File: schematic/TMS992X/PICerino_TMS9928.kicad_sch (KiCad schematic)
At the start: 75 parts, among them CON1 PICERINO-EDGE, J1 Conn_01x02, J10 Conn_01x03, J2 Conn_01x03, J3 Conn_01x03, J4 Conn_01x03, J5 Y, J6 Yr, J7 Yb, J8 Conn_01x08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

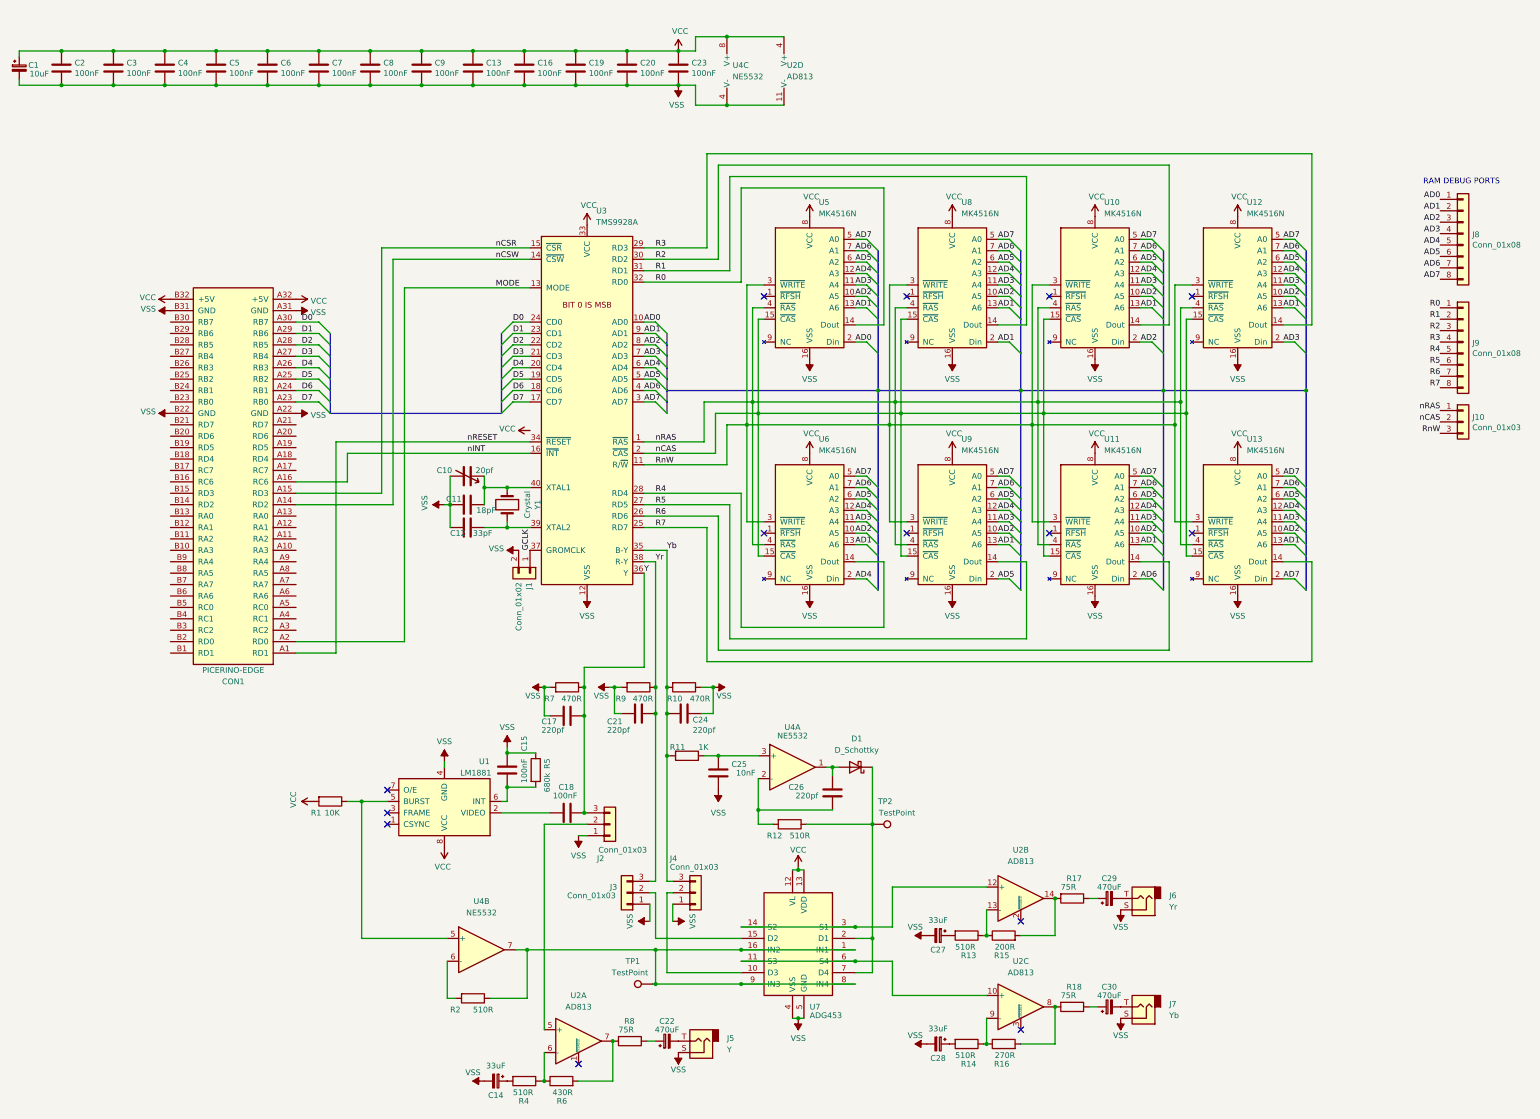
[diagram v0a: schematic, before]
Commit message: added new switch and sample video chip to simplify video output. work in progress.
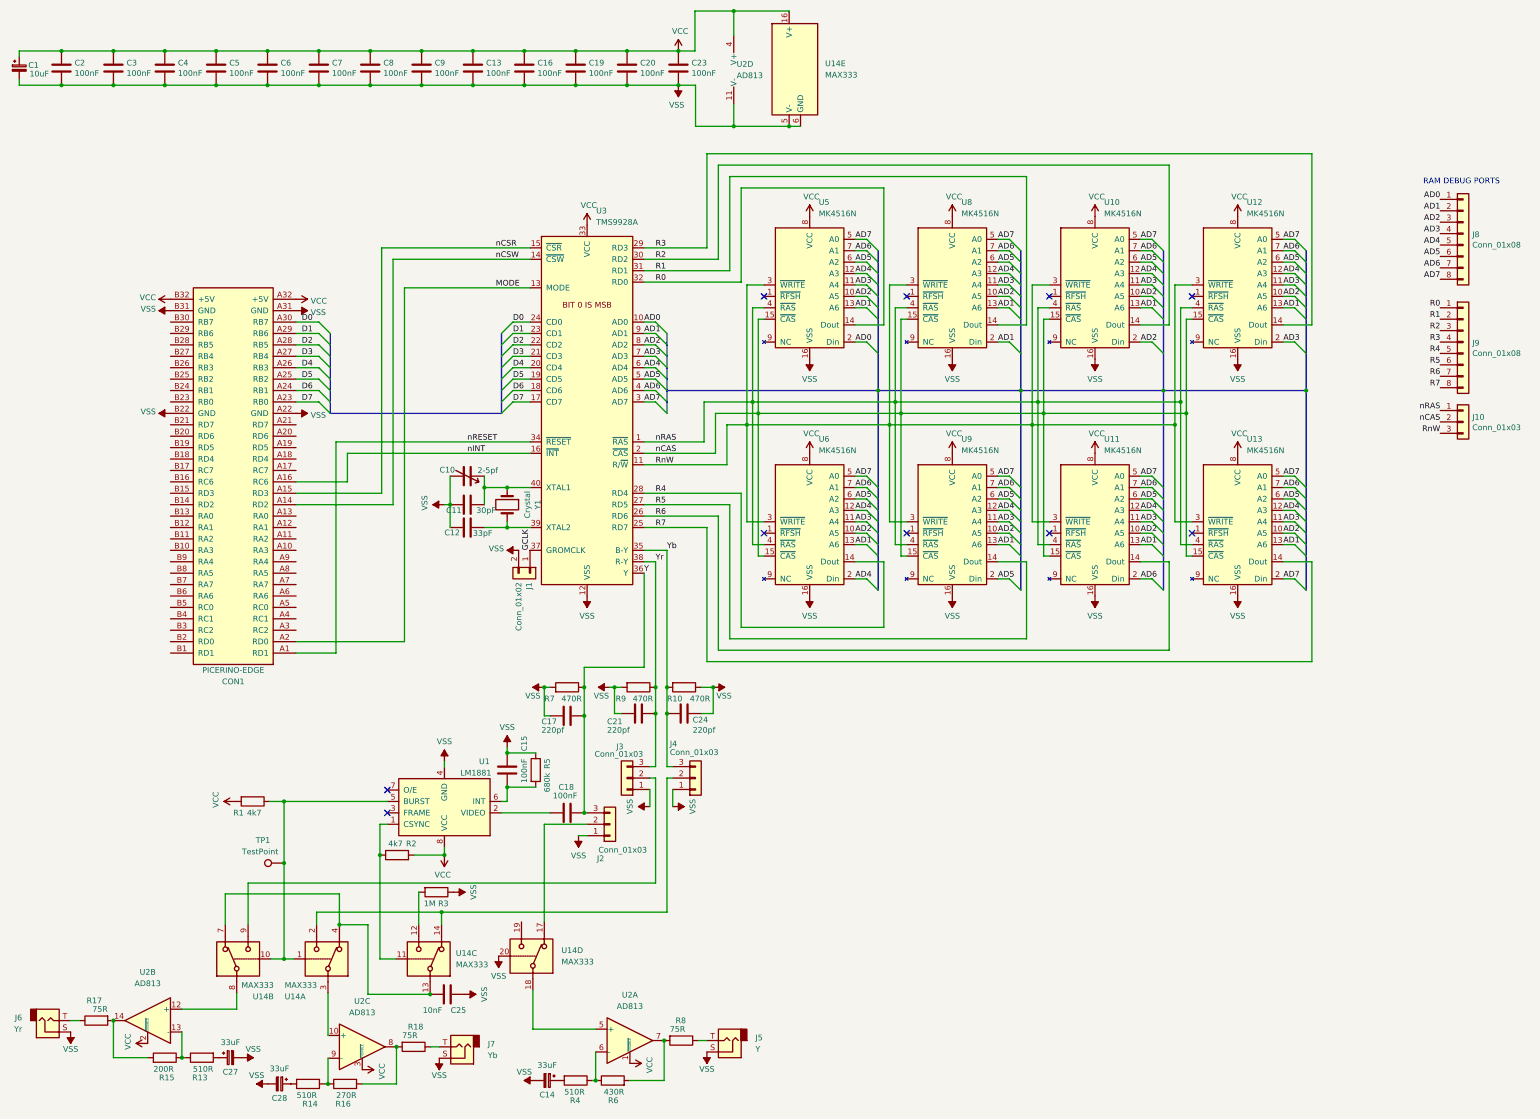
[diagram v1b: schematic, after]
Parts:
- removed C22, C29, C30: 470uF, Capacitor_THT:CP_Radial_D8.0mm_P5.00mm, symbol Device:CP_Small
- removed C26: 220pf, Capacitor_THT:C_Disc_D4.7mm_W2.5mm_P5.00mm, symbol Device:C
- removed D1: D_Schottky, Diode_THT:D_DO-35_SOD27_P7.62mm_Horizontal, symbol Device:D_Schottky
- removed R11: 1K, Resistor_THT:R_Axial_DIN0207_L6.3mm_D2.5mm_P7.62mm_Horizontal, symbol Device:R
- removed R12: 510R, Resistor_THT:R_Axial_DIN0207_L6.3mm_D2.5mm_P7.62mm_Horizontal, symbol Device:R
- removed TP2: TestPoint, Connector_PinHeader_2.54mm:PinHeader_1x01_P2.54mm_Vertical, symbol Connector:TestPoint
- removed U4: NE5532, Package_DIP:DIP-8_W7.62mm_LongPads, symbol Amplifier_Operational:NE5532
- removed U7: ADG453, Package_DIP:DIP-16_W7.62mm_LongPads, symbol Analog_Switch_II:ADG453
- added R3: 1M, Resistor_THT:R_Axial_DIN0207_L6.3mm_D2.5mm_P7.62mm_Horizontal, symbol Device:R
- added U14: MAX333, symbol Analog_Switch:MAX333
- C10: value 20pf -> 2-5pf
- C11: value 18pF -> 30pF
- R1: value 10K -> 4k7
- R2: value 510R -> 4k7
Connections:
- net VCC: now also R2.2, U2.1 (~{DISABLE}), U2.2 (~{DISABLE}), U2.3 (~{DISABLE}), U14.16 (V+)
- net VSS: now also C25.1, R3.1, U14.20, U14.5 (V-), U14.6 (GND); no longer C25.2
- net at R1.1, U1.5 (BURST): now also TP1.1, U14.1, U14.10
- net at U1.1 (CSYNC): now also R2.1, U14.11
- net at J2.2 (Pin_2): now also U14.17; no longer U2.5 (+)
- net at J4.2 (Pin_2): now also U14.14, U14.2
- net at J3.2 (Pin_2): now also U14.9
- net at J7.T: now also R18.1
- net at R17.1: now also J6.T
- net at R8.1: now also J5.T
- net at U2.10 (+): now also U14.3
- net at U2.12 (+): now also U14.8
- new net: R3.2, U14.12
- new net: C25.2, U14.13, U14.4, U14.7
- new net: U14.18, U2.5 (+)
- no-connect marks 14 -> 10
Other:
- moved on the sheet: C14, C27, C28, J3, J4, J5, J6, J7, R1, R13, R14, R15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

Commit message: initial commit of v2 tms992X board
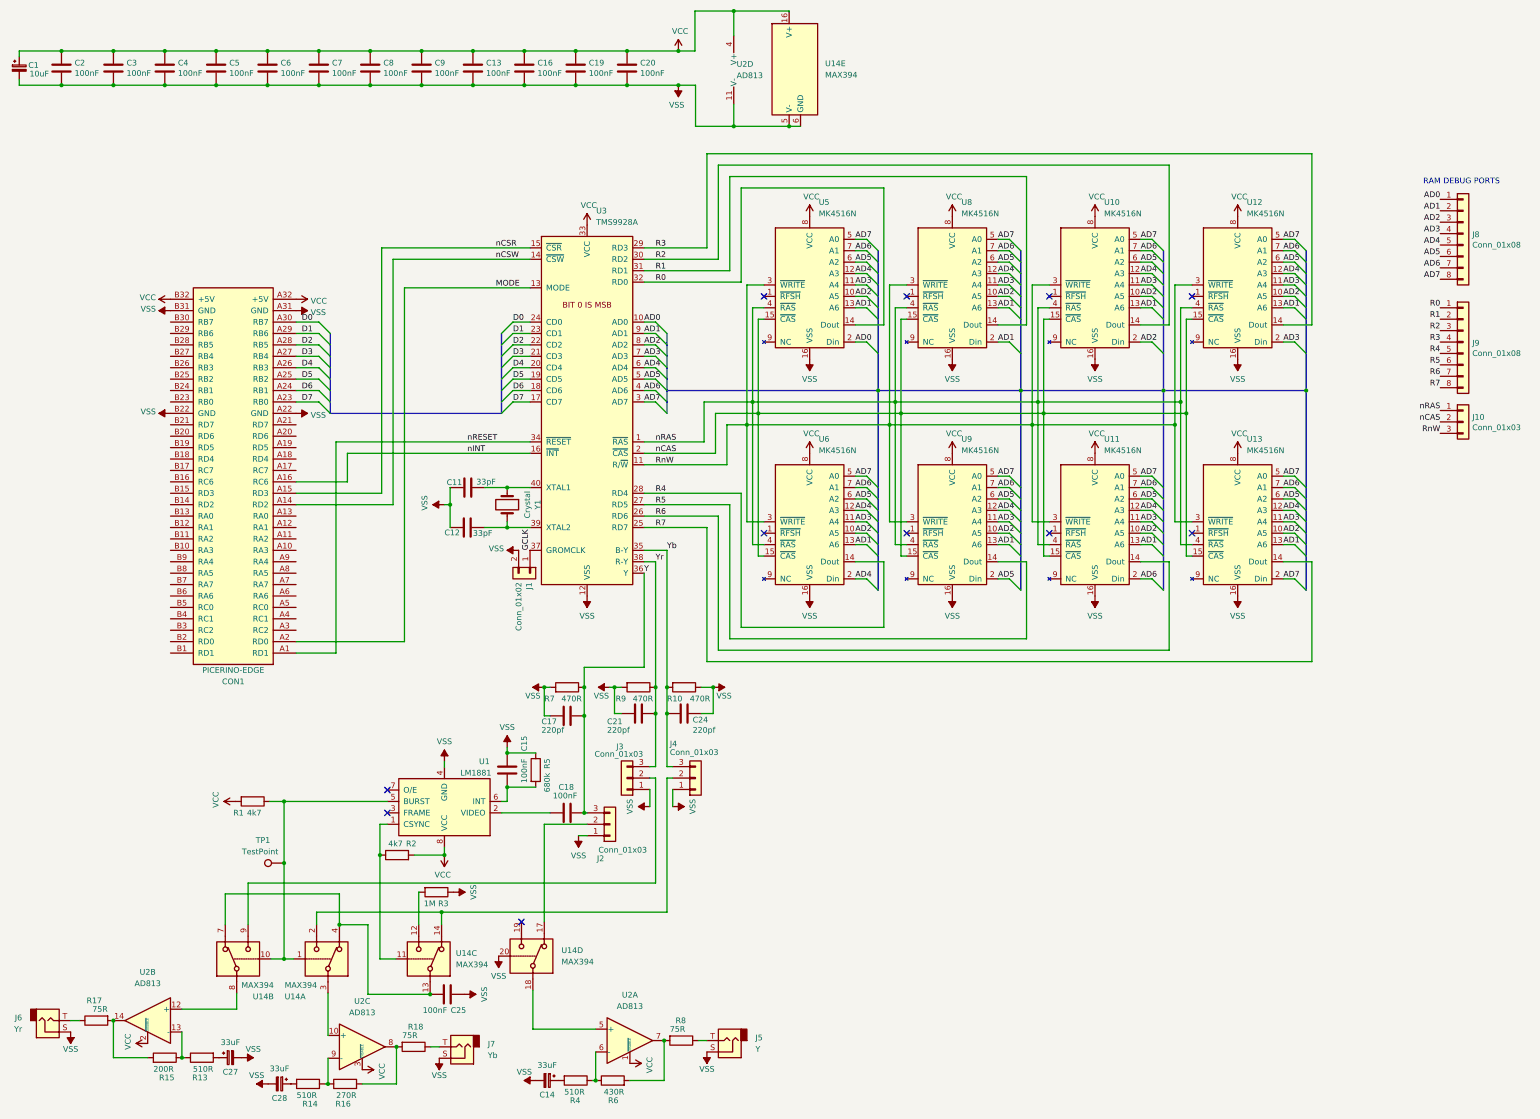
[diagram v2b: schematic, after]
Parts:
- removed C10: 2-5pf, Capacitor_THT:C_Rect_L10.0mm_W5.0mm_P5.00mm_P7.50mm, symbol Device:C_Variable
- removed C23: 100nF, Capacitor_THT:C_Disc_D4.7mm_W2.5mm_P5.00mm, symbol Device:C
- C11: value 30pF -> 33pF
- C25: value 10nF -> 100nF
- U14: value MAX333 -> MAX394; footprint (none) -> Package_DIP:DIP-20_W7.62mm_LongPads
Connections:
- no-connect marks 10 -> 11
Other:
- moved on the sheet: C11
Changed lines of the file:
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@@
   (junction (at 75.565 27.305) (diameter 0) (color 0 0 0 0)
   )
-  (junction (at 123.825 124.46) (diameter 0) (color 0 0 0 0)
-  )
   (junction (at 100.584 206.248) (diameter 0) (color 0 0 0 0)
   )
@@
   (no_connect (at 217.805 81.915))
   (no_connect (at 186.055 134.62))
+  (no_connect (at 132.08 221.107))
   (bus_entry (at 208.915 74.295) (size 2.54 2.54)
     (stroke (width 0) (type default))
@@
     (stroke (width 0) (type default))
   )
-  (wire (pts (xy 116.205 121.92) (xy 116.205 128.27))
-    (stroke (width 0) (type default))
-  )
   (wire (pts (xy 175.895 52.705) (xy 276.225 52.705))
     (stroke (width 0) (type default))
@@
     (stroke (width 0) (type default))
   )
-  (wire (pts (xy 123.825 124.46) (xy 123.825 121.92))
-    (stroke (width 0) (type default))
-  )
   (wire (pts (xy 97.917 237.236) (xy 111.76 237.236))
     (stroke (width 0) (type default))
@@
     (stroke (width 0) (type default))
   )
+  (wire (pts (xy 116.332 124.46) (xy 116.205 124.46))
+    (stroke (width 0) (type default))
+  )
   (wire (pts (xy 160.655 186.563) (xy 161.925 186.563))
     (stroke (width 0) (type default))
@@
     (stroke (width 0) (type default))
   )
-  (wire (pts (xy 123.825 124.46) (xy 128.905 124.46))
+  (wire (pts (xy 123.952 124.46) (xy 128.905 124.46))
     (stroke (width 0) (type default))
   )
@@
     (stroke (width 0) (type default))
   )
+  (wire (pts (xy 116.205 124.46) (xy 116.205 128.27))
+    (stroke (width 0) (type default))
+  )
   (bus (pts (xy 211.455 124.46) (xy 211.455 127))
     (stroke (width 0) (type default))
@@
     (stroke (width 0) (type default))
   )
-  (wire (pts (xy 123.825 128.27) (xy 123.825 124.46))
-    (stroke (width 0) (type default))
-  )
   (bus (pts (xy 164.465 95.25) (xy 164.465 97.79))
     (stroke (width 0) (type default))
@@
     )
   )
-  (symbol (lib_id "Device:C") (at 120.015 128.27 90) (unit 1)
+  (symbol (lib_id "Device:C") (at 120.142 124.46 90) (unit 1)
     (in_bom yes) (on_board yes) (dnp no)
-    (property "Reference" "C11" (at 118.745 129.54 90)
+    (property "Reference" "C11" (at 118.872 123.317 90)
       (effects (font (size 1.27 1.27)) (justify left))
     )
-    (property "Value" "30pF" (at 126.365 129.54 90)
+    (property "Value" "33pF" (at 126.365 123.19 90)
       (effects (font (size 1.27 1.27)) (justify left))
     )
-    (property "Footprint" "Capacitor_THT:C_Disc_D3.0mm_W1.6mm_P2.50mm" (at 123.825 127.3048 0)
+    (property "Footprint" "Capacitor_THT:C_Disc_D3.0mm_W1.6mm_P2.50mm" (at 123.952 123.4948 0)
       (effects (font (size 1.27 1.27)) hide)
     )
-    (property "Datasheet" "~" (at 120.015 128.27 0)
+    (property "Datasheet" "~" (at 120.142 124.46 0)
       (effects (font (size 1.27 1.27)) hide)
     )
@@
     )
   )
-  (symbol (lib_id "Device:C") (at 167.005 31.115 0) (unit 1)
-    (in_bom yes) (on_board yes) (dnp no)
-    (property "Reference" "C23" (at 169.926 29.9466 0)
-      (effects (font (size 1.27 1.27)) (justify left))
-    )
-    (property "Value" "100nF" (at 169.926 32.258 0)
-      (effects (font (size 1.27 1.27)) (justify left))
-    )
-    (property "Footprint" "Capacitor_THT:C_Disc_D4.7mm_W2.5mm_P5.00mm" (at 167.9702 34.925 0)
-      (effects (font (size 1.27 1.27)) hide)
-    )
-    (property "Datasheet" "~" (at 167.005 31.115 0)
-      (effects (font (size 1.27 1.27)) hide)
-    )
-    (pin "1")
-    (pin "2")
-    (instances
-      (project "PICerino_TMS9928"
-        (path "/01e9b6e7-adf9-4ee7-9447-a588630ee4a2"
-          (reference "C23") (unit 1)
-        )
-      )
-    )
-  )
   (symbol (lib_id "Device:C") (at 155.575 31.115 0) (unit 1)
     (in_bom yes) (on_board yes) (dnp no)
@@
     )
   )
-  (symbol (lib_id "Device:C_Variable") (at 120.015 121.92 270) (unit 1)
-    (in_bom yes) (on_board yes) (dnp no)
-    (property "Reference" "C10" (at 115.57 120.523 90)
-      (effects (font (size 1.27 1.27)))
-    )
-    (property "Value" "2-5pf" (at 124.587 120.65 90)
-      (effects (font (size 1.27 1.27)))
-    )
-    (property "Footprint" "Capacitor_THT:C_Rect_L10.0mm_W5.0mm_P5.00mm_P7.50mm" (at 120.015 121.92 0)
-      (effects (font (size 1.27 1.27)) hide)
-    )
-    (property "Datasheet" "~" (at 120.015 121.92 0)
-      (effects (font (size 1.27 1.27)) hide)
-    )
-    (pin "1")
-    (pin "2")
-    (instances
-      (project "PICerino_TMS9928"
-        (path "/01e9b6e7-adf9-4ee7-9447-a588630ee4a2"
-          (reference "C10") (unit 1)
-        )
-      )
-    )
-  )
   (symbol (lib_id "Connector_Generic:Conn_01x08") (at 341.63 67.945 0) (unit 1)
     (in_bom yes) (on_board yes) (dnp no)
@@
       (effects (font (size 1.27 1.27)) (justify left))
     )
-    (property "Value" "MAX333" (at 117.475 230.632 90)
+    (property "Value" "MAX394" (at 117.475 230.632 90)
       (effects (font (size 1.27 1.27)) (justify left))
     )
-    (property "Footprint" "" (at 114.3 229.362 0)
+    (property "Footprint" "Package_DIP:DIP-20_W7.62mm_LongPads" (at 114.3 229.362 0)
       (effects (font (size 1.27 1.27)) hide)
     )
@@
       (effects (font (size 1.27 1.27)) (justify left))
     )
-    (property "Value" "MAX333" (at 140.97 229.997 90)
+    (property "Value" "MAX394" (at 140.97 229.997 90)
       (effects (font (size 1.27 1.27)) (justify left))
     )
-    (property "Footprint" "" (at 137.16 228.727 0)
+    (property "Footprint" "Package_DIP:DIP-20_W7.62mm_LongPads" (at 137.16 228.727 0)
       (effects (font (size 1.27 1.27)) hide)
     )
@@
       (effects (font (size 1.27 1.27)) (justify left))
     )
-    (property "Value" "10nF" (at 110.109 240.792 90)
+    (property "Value" "100nF" (at 110.109 240.792 90)
       (effects (font (size 1.27 1.27)) (justify left))
     )
@@
       (effects (font (size 1.27 1.27)) (justify left))
     )
-    (property "Value" "MAX333" (at 199.644 32.639 0)
+    (property "Value" "MAX394" (at 199.644 32.639 0)
       (effects (font (size 1.27 1.27)) (justify left))
     )
-    (property "Footprint" "" (at 191.643 31.369 0)
+    (property "Footprint" "Package_DIP:DIP-20_W7.62mm_LongPads" (at 191.643 31.369 0)
       (effects (font (size 1.27 1.27)) hide)
     )
@@
       (effects (font (size 1.27 1.27)) (justify left))
     )
-    (property "Value" "MAX333" (at 76.962 235.204 90)
+    (property "Value" "MAX394" (at 76.962 235.204 90)
       (effects (font (size 1.27 1.27)) (justify left))
     )
-    (property "Footprint" "" (at 66.167 229.362 0)
+    (property "Footprint" "Package_DIP:DIP-20_W7.62mm_LongPads" (at 66.167 229.362 0)
       (effects (font (size 1.27 1.27)) hide)
     )
@@
       (effects (font (size 1.27 1.27)) (justify left))
     )
-    (property "Value" "MAX333" (at 79.375 235.204 90)
+    (property "Value" "MAX394" (at 79.375 235.204 90)
       (effects (font (size 1.27 1.27)) (justify left))
     )
-    (property "Footprint" "" (at 91.567 229.362 0)
+    (property "Footprint" "Package_DIP:DIP-20_W7.62mm_LongPads" (at 91.567 229.362 0)
       (effects (font (size 1.27 1.27)) hide)
     )
